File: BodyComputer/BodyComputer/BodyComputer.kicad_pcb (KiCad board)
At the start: 2 copper layers, 0 parts

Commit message: Update due to moving to another computer. Updated Schematic, Print-outs, PCB in development
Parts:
- added BZ1: Buzzer, Buzzer_Beeper:Buzzer_12x9.5RM7.6, F.Cu at (274.8, 30.0)
- added C1: 47u, Capacitor_SMD:CP_Elec_6.3x9.9, F.Cu at (124.5, 141.6)
- added C10: 1u, Capacitor_SMD:C_0603_1608Metric, F.Cu at (89.7, 134.0)
- added C11: 47u, Capacitor_SMD:CP_Elec_6.3x9.9, F.Cu at (140.3, 129.5)
- added C12: 100u, Capacitor_SMD:CP_Elec_6.3x9.9, F.Cu at (70.5, 131.4)
- added C13: 1m, Capacitor_SMD:CP_Elec_10x12.5, F.Cu at (81.3, 130.2)
- added C14: 10n, Capacitor_SMD:C_0603_1608Metric, F.Cu at (382.2, 93.9)
- added C15: 100n, Capacitor_SMD:C_0603_1608Metric, F.Cu at (364.3, 95.7)
- added C16: 1u, Capacitor_SMD:C_0603_1608Metric, F.Cu at (390.7, 87.5)
- added C17: 10n, Capacitor_SMD:C_0603_1608Metric, F.Cu at (368.3, 95.7)
- added C18: 10n, Capacitor_SMD:C_0603_1608Metric, F.Cu at (398.3, 78.4)
- added C19: 100n, Capacitor_SMD:C_0603_1608Metric, F.Cu at (372.3, 95.7)
- added C2: 330u, Capacitor_SMD:CP_Elec_10x12.5, F.Cu at (113.0, 139.7)
- added C20: 100n, Capacitor_SMD:C_0603_1608Metric, F.Cu at (376.3, 95.7)
- added C21: 10n, Capacitor_SMD:C_0603_1608Metric, F.Cu at (217.9, 82.6)
- added C22: 100n, Capacitor_SMD:C_0603_1608Metric, F.Cu at (221.9, 82.6)
- added C23: 1u, Capacitor_SMD:C_0603_1608Metric, F.Cu at (213.9, 82.6)
- added C24: 100n, Capacitor_SMD:C_0603_1608Metric, F.Cu at (225.9, 82.6)
- added C25: 10n, Capacitor_SMD:C_0603_1608Metric, F.Cu at (386.8, 114.4)
- added C26: 100n, Capacitor_SMD:C_0603_1608Metric, F.Cu at (382.7, 114.4)
- added C27: 1u, Capacitor_SMD:C_0603_1608Metric, F.Cu at (382.7, 116.9)
- added C28: 10n, Capacitor_SMD:C_0603_1608Metric, F.Cu at (395.6, 107.2)
- added C29: 100n, Capacitor_SMD:C_0603_1608Metric, F.Cu at (399.6, 104.7)
- added C3: 100n, Capacitor_SMD:C_0603_1608Metric, F.Cu at (133.3, 142.9)
- added C30: 1u, Capacitor_SMD:C_0603_1608Metric, F.Cu at (386.8, 116.9)
- added C31: 10p, Capacitor_SMD:C_0603_1608Metric, F.Cu at (391.5, 111.8)
- added C32: 10p, Capacitor_SMD:C_0603_1608Metric, F.Cu at (381.1, 123.1)
- added C33: 100n, Capacitor_SMD:C_0603_1608Metric, F.Cu at (385.4, 119.5)
- added C34: 100n, Capacitor_SMD:C_0603_1608Metric, F.Cu at (395.5, 112.2)
- added C35: 100n, Capacitor_SMD:C_0603_1608Metric, F.Cu at (387.5, 111.8)
- added C36: 100n, Capacitor_SMD:C_0603_1608Metric, F.Cu at (395.5, 109.7)
- added C37: 100n, Capacitor_SMD:C_0603_1608Metric, F.Cu at (399.6, 107.2)
- added C38: 100n, Capacitor_SMD:C_0603_1608Metric, F.Cu at (342.3, 110.0)
- added C39: 100n, Capacitor_SMD:C_0603_1608Metric, F.Cu at (352.8, 99.0)
- added C4: 100n, Capacitor_SMD:C_0603_1608Metric, F.Cu at (130.2, 142.9)
- added C40: 100n, Capacitor_SMD:C_0603_1608Metric, F.Cu at (346.3, 107.5)
- added C41: 100n, Capacitor_SMD:C_0603_1608Metric, F.Cu at (340.2, 113.2)
- added C42: 100n, Capacitor_SMD:C_0603_1608Metric, F.Cu at (333.3, 117.8)
- added C43: 100n, Capacitor_SMD:C_0603_1608Metric, F.Cu at (342.3, 107.5)
- added C44: 100n, Capacitor_SMD:C_0603_1608Metric, F.Cu at (351.2, 94.0)
- added C45: 100n, Capacitor_SMD:C_0603_1608Metric, F.Cu at (344.8, 99.9)
- added C46: 100n, Capacitor_SMD:C_0603_1608Metric, F.Cu at (332.2, 112.8)
- added C47: 100n, Capacitor_SMD:C_0603_1608Metric, F.Cu at (338.3, 105.7)
- added C48: 100n, Capacitor_SMD:C_0603_1608Metric, F.Cu at (348.8, 97.0)
- added C49: 100n, Capacitor_SMD:C_0603_1608Metric, F.Cu at (338.3, 108.2)
- added C5: 1u, Capacitor_SMD:C_0603_1608Metric, F.Cu at (130.2, 139.1)
- added C50: 100n, Capacitor_SMD:C_0603_1608Metric, F.Cu at (348.8, 102.0)
- added C51: 100n, Capacitor_SMD:C_0603_1608Metric, F.Cu at (332.2, 115.3)
- added C52: 100n, Capacitor_SMD:C_0603_1608Metric, F.Cu at (344.8, 102.4)
- added C6: 10n, Capacitor_SMD:C_0603_1608Metric, F.Cu at (89.7, 130.8)
- added C7: 100n, Capacitor_SMD:C_0603_1608Metric, F.Cu at (133.3, 139.7)
- added C8: 100n, Capacitor_SMD:C_0603_1608Metric, F.Cu at (89.7, 127.6)
- added C9: 1u, Capacitor_SMD:C_0603_1608Metric, F.Cu at (133.3, 136.5)
- added D1: Transil, Diode_SMD:D_SMB_Handsoldering, F.Cu at (41.3, 141.6)
- added D10: LED, Diode_SMD:D_0603_1608Metric_Pad1.05x0.95mm_HandSolder, F.Cu at (121.9, 129.3)
- added D11: LED, Diode_SMD:D_0603_1608Metric_Pad1.05x0.95mm_HandSolder, F.Cu at (209.7, 82.6)
- added D12: D, Diode_SMD:D_SMA, F.Cu at (35.3, 77.2)
- added D13: D, Diode_SMD:D_SMA, F.Cu at (35.3, 55.4)
- added D14: D, Diode_SMD:D_SMA, F.Cu at (35.3, 84.8)
- added D15: D, Diode_SMD:D_SMA, F.Cu at (35.3, 47.8)
- added D16: D, Diode_SMD:D_SMA, F.Cu at (35.3, 99.5)
- added D17: D, Diode_SMD:D_SMA, F.Cu at (15.0, 37.6)
- added D18: D, Diode_SMD:D_SMA, F.Cu at (35.3, 91.9)
- added D19: D, Diode_SMD:D_SMA, F.Cu at (15.0, 30.0)
- added D2: D, Diode_SMD:D_SMC_Handsoldering, F.Cu at (52.1, 142.2)
- added D20: D, Diode_SMD:D_SMA, F.Cu at (35.3, 70.1)
- added D21: D, Diode_SMD:D_SMA, F.Cu at (35.3, 62.5)
- added D22: D, Diode_SMD:D_SMA, F.Cu at (15.0, 67.1)
- added D23: D_Zener, Diode_SMD:D_SOD-323_HandSoldering, F.Cu at (35.6, 113.0)
- added D24: D_Zener, Diode_SMD:D_SOD-323_HandSoldering, F.Cu at (35.6, 107.4)
- added D25: D, Diode_SMD:D_SMA, F.Cu at (15.0, 59.4)
- added D26: D_Zener, Diode_SMD:D_SOD-323_HandSoldering, F.Cu at (37.1, 29.0)
- added D27: D_Zener, Diode_SMD:D_SOD-323_HandSoldering, F.Cu at (37.1, 34.6)
- added D28: D_Zener, Diode_SMD:D_SOD-323_HandSoldering, F.Cu at (37.1, 40.4)
- added D29: D, Diode_SMD:D_SMA, F.Cu at (15.0, 81.8)
- added D3: D_Zener, Diode_SMD:D_SOD-323_HandSoldering, F.Cu at (40.0, 132.7)
- added D30: D, Diode_SMD:D_SMA, F.Cu at (15.0, 74.2)
- added D31: D, Diode_SMD:D_SMA, F.Cu at (15.0, 52.3)
- added D32: D_Zener, Diode_SMD:D_SOD-323_HandSoldering, F.Cu at (54.9, 29.0)
- added D33: D_Zener, Diode_SMD:D_SOD-323_HandSoldering, F.Cu at (54.9, 34.6)
- added D34: D_Zener, Diode_SMD:D_SOD-323_HandSoldering, F.Cu at (54.9, 40.4)
- added D35: D, Diode_SMD:D_SMA, F.Cu at (15.0, 44.7)
- added D36: LED, Diode_SMD:D_0603_1608Metric_Pad1.05x0.95mm_HandSolder, F.Cu at (383.3, 109.4)
- added D37: LED, Diode_SMD:D_0603_1608Metric_Pad1.05x0.95mm_HandSolder, F.Cu at (369.2, 120.6)
- added D38: LED, Diode_SMD:D_0603_1608Metric_Pad1.05x0.95mm_HandSolder, F.Cu at (360.5, 120.6)
- added D39: LED, Diode_SMD:D_0603_1608Metric_Pad1.05x0.95mm_HandSolder, F.Cu at (379.0, 109.4)
- added D4: D, Diode_SMD:D_SMC_Handsoldering, F.Cu at (67.3, 142.2)
- added D40: LED, Diode_SMD:D_0603_1608Metric_Pad1.05x0.95mm_HandSolder, F.Cu at (364.9, 120.6)
- added D41: LED, Diode_SMD:D_0603_1608Metric_Pad1.05x0.95mm_HandSolder, F.Cu at (360.5, 123.2)
- added D42: LED, Diode_SMD:D_0603_1608Metric_Pad1.05x0.95mm_HandSolder, F.Cu at (395.8, 102.1)
- added D43: LED, Diode_SMD:D_0603_1608Metric_Pad1.05x0.95mm_HandSolder, F.Cu at (364.9, 123.2)
- added D44: D_Zener_3V3, Diode_SMD:D_SOD-323_HandSoldering, F.Cu at (325.7, 107.5)
- added D45: D_Zener_3V3, Diode_SMD:D_SOD-323_HandSoldering, F.Cu at (332.2, 101.3)
- added D46: D_Zener_3V3, Diode_SMD:D_SOD-323_HandSoldering, F.Cu at (343.7, 89.2)
- added D47: D_Zener_3V3, Diode_SMD:D_SOD-323_HandSoldering, F.Cu at (338.6, 89.2)
- added D48: D_Zener_3V3, Diode_SMD:D_SOD-323_HandSoldering, F.Cu at (302.6, 118.3)
- added D49: D_Zener_3V3, Diode_SMD:D_SOD-323_HandSoldering, F.Cu at (307.7, 118.3)
- added D5: D, Diode_SMD:D_SMC_Handsoldering, F.Cu at (82.5, 142.2)
- added D50: D_Zener_3V3, Diode_SMD:D_SOD-323_HandSoldering, F.Cu at (320.7, 107.5)
- added D51: D_Zener_3V3, Diode_SMD:D_SOD-323_HandSoldering, F.Cu at (332.2, 98.4)
- added D52: D_Zener_3V3, Diode_SMD:D_SOD-323_HandSoldering, F.Cu at (338.6, 92.2)
- added D53: D_Zener_3V3, Diode_SMD:D_SOD-323_HandSoldering, F.Cu at (297.6, 118.3)
- added D54: D_Zener_3V3, Diode_SMD:D_SOD-323_HandSoldering, F.Cu at (320.7, 110.5)
- added D55: D_Zener_3V3, Diode_SMD:D_SOD-323_HandSoldering, F.Cu at (312.7, 118.3)
- added D56: D_Zener, Diode_SMD:D_SOD-323_HandSoldering, F.Cu at (63.2, 92.7)
- added D57: D_Zener, Diode_SMD:D_SOD-323_HandSoldering, F.Cu at (63.2, 98.1)
- added D6: D, Diode_SMD:D_SMC_Handsoldering, F.Cu at (97.8, 142.2)
- added D7: D_Zener, Diode_SMD:D_SOD-323_HandSoldering, F.Cu at (134.0, 128.9)
- added D8: LED, Diode_SMD:D_0603_1608Metric_Pad1.05x0.95mm_HandSolder, F.Cu at (125.7, 129.3)
- added D9: LED, Diode_SMD:D_0603_1608Metric_Pad1.05x0.95mm_HandSolder, F.Cu at (129.5, 129.3)
- added F1: Fuse, SamacSys_Parts:FuseHolder22mm, F.Cu at (35.6, 143.5)
- added J1: Screw_Terminal_01x02, SamacSys_Parts:SHDR2W99P0X500_1X2_1000X760X1000P, F.Cu at (7.62, 136.5)
- added J10: Conn_02x03_Odd_Even, Connector_IDC:IDC-Header_2x03_P2.54mm_Vertical, F.Cu at (254.1, 53.2)
- added J11: SS-6488-FLS, SamacSys_Parts:SS6488FLS, F.Cu at (165.4, 84.3)
- added J12: USB_B_Mini, Connector_USB:USB_Mini-B_Wuerth_65100516121_Horizontal, F.Cu at (245.6, 74.1)
- added J13: Conn_02x05_Odd_Even, Connector_IDC:IDC-Header_2x05_P2.54mm_Vertical, F.Cu at (265.3, 51.6)
- added J14: Conn_02x05_Odd_Even, Connector_IDC:IDC-Header_2x05_P2.54mm_Vertical, F.Cu at (265.3, 29.4)
- added J15: Screw_Terminal_01x02, SamacSys_Parts:SHDR2W99P0X500_1X2_1000X760X1000P, F.Cu at (27.9, 78.5)
- added J16: Screw_Terminal_01x02, SamacSys_Parts:SHDR2W99P0X500_1X2_1000X760X1000P, F.Cu at (27.9, 54.1)
- added J17: Screw_Terminal_01x02, SamacSys_Parts:SHDR2W99P0X500_1X2_1000X760X1000P, F.Cu at (27.9, 98.3)
- added J18: Screw_Terminal_01x02, SamacSys_Parts:SHDR2W99P0X500_1X2_1000X760X1000P, F.Cu at (7.62, 36.3)
- added J19: Screw_Terminal_01x02, SamacSys_Parts:SHDR2W99P0X500_1X2_1000X760X1000P, F.Cu at (48.5, 112.3)
- added J2: Screw_Terminal_01x02, SamacSys_Parts:SHDR2W99P0X500_1X2_1000X760X1000P, F.Cu at (7.62, 125.7)
- added J20: Screw_Terminal_01x02, SamacSys_Parts:SHDR2W99P0X500_1X2_1000X760X1000P, F.Cu at (27.9, 68.8)
- added J21: Screw_Terminal_01x02, SamacSys_Parts:SHDR2W99P0X500_1X2_1000X760X1000P, F.Cu at (54.4, 98.4)
- added J22: Screw_Terminal_01x03, SamacSys_Parts:SHDR3W95P0X500_1X3_1620X900X1280P, F.Cu at (27.9, 40.1)
- added J23: Screw_Terminal_01x02, SamacSys_Parts:SHDR2W99P0X500_1X2_1000X760X1000P, F.Cu at (7.62, 65.8)
- added J24: Screw_Terminal_01x02, SamacSys_Parts:SHDR2W99P0X500_1X2_1000X760X1000P, F.Cu at (7.62, 80.5)
- added J25: Screw_Terminal_01x03, SamacSys_Parts:SHDR3W95P0X500_1X3_1620X900X1280P, F.Cu at (45.5, 40.1)
- added J26: Screw_Terminal_01x02, SamacSys_Parts:SHDR2W99P0X500_1X2_1000X760X1000P, F.Cu at (7.62, 51.1)
- added J27: Screw_Terminal_01x02, SamacSys_Parts:SHDR2W99P0X500_1X2_1000X760X1000P, F.Cu at (298.3, 103.1)
- added J28: Screw_Terminal_01x02, SamacSys_Parts:SHDR2W99P0X500_1X2_1000X760X1000P, F.Cu at (316.3, 92.3)
- added J29: Screw_Terminal_01x02, SamacSys_Parts:SHDR2W99P0X500_1X2_1000X760X1000P, F.Cu at (298.3, 112.2)
- added J3: Screw_Terminal_01x03, SamacSys_Parts:SHDR3W95P0X500_1X3_1620X900X1280P, F.Cu at (7.62, 114.3)
- added J30: Screw_Terminal_01x02, SamacSys_Parts:SHDR2W99P0X500_1X2_1000X760X1000P, F.Cu at (309.9, 103.1)
- added J31: Screw_Terminal_01x02, SamacSys_Parts:SHDR2W99P0X500_1X2_1000X760X1000P, F.Cu at (327.8, 92.3)
- added J32: Screw_Terminal_01x03, SamacSys_Parts:SHDR3W95P0X500_1X3_1620X900X1280P, F.Cu at (299.1, 93.5)
- added J33: Screw_Terminal_01x02, SamacSys_Parts:SHDR2W99P0X500_1X2_1000X760X1000P, F.Cu at (309.9, 112.2)
- added J34: Screw_Terminal_01x02, SamacSys_Parts:SHDR2W99P0X500_1X2_1000X760X1000P, F.Cu at (321.4, 101.5)
- added J35: Conn_01x02, Connector_PinSocket_2.54mm:PinSocket_1x02_P2.54mm_Vertical, F.Cu at (-6.86, 132.3)
- added J4: Screw_Terminal_01x03, SamacSys_Parts:SHDR3W95P0X500_1X3_1620X900X1280P, F.Cu at (7.62, 97.2)
- added J5: Screw_Terminal_01x03, SamacSys_Parts:SHDR3W95P0X500_1X3_1620X900X1280P, F.Cu at (27.9, 132.7)
- added J6: Screw_Terminal_01x03, SamacSys_Parts:SHDR3W95P0X500_1X3_1620X900X1280P, F.Cu at (27.9, 114.9)
- added J7: MicroSD, SamacSys_Parts:1140084168, F.Cu at (388.2, 78.5)
- added J8: SS-6488-FLS, SamacSys_Parts:SS6488FLS, F.Cu at (94.5, 33.3)
- added J9: Conn_02x05_Odd_Even, Connector_IDC:IDC-Header_2x05_P2.54mm_Vertical, F.Cu at (243.4, 53.2)
- added Q1: Q_NPN_BCE, Package_TO_SOT_SMD:SOT-23, F.Cu at (287.6, 25.5)
- added Q10: IRLML2060, Package_TO_SOT_SMD:SOT-23, F.Cu at (39.4, 68.6)
- added Q11: IRLML2060, Package_TO_SOT_SMD:SOT-23, F.Cu at (39.4, 61.0)
- added Q12: IRLML2060, Package_TO_SOT_SMD:SOT-23, F.Cu at (19.1, 65.5)
- added Q13: IRLML2060, Package_TO_SOT_SMD:SOT-23, F.Cu at (19.1, 57.9)
- added Q14: IRLML2060, Package_TO_SOT_SMD:SOT-23, F.Cu at (19.1, 80.3)
- added Q15: IRLML2060, Package_TO_SOT_SMD:SOT-23, F.Cu at (19.1, 72.6)
- added Q16: IRLML2060, Package_TO_SOT_SMD:SOT-23, F.Cu at (19.1, 50.8)
- added Q17: IRLML2060, Package_TO_SOT_SMD:SOT-23, F.Cu at (19.1, 43.2)
- added Q2: IRLML2060, Package_TO_SOT_SMD:SOT-23, F.Cu at (39.4, 75.7)
- added Q3: IRLML2060, Package_TO_SOT_SMD:SOT-23, F.Cu at (39.4, 53.8)
- added Q4: IRLML2060, Package_TO_SOT_SMD:SOT-23, F.Cu at (39.4, 83.3)
- added Q5: IRLML2060, Package_TO_SOT_SMD:SOT-23, F.Cu at (39.4, 46.2)
- added Q6: IRLML2060, Package_TO_SOT_SMD:SOT-23, F.Cu at (39.4, 98.0)
- added Q7: IRLML2060, Package_TO_SOT_SMD:SOT-23, F.Cu at (19.1, 36.1)
- added Q8: IRLML2060, Package_TO_SOT_SMD:SOT-23, F.Cu at (39.6, 90.4)
- added Q9: IRLML2060, Package_TO_SOT_SMD:SOT-23, F.Cu at (19.1, 28.4)
- added R1: 4,7k, Resistor_SMD:R_0603_1608Metric, F.Cu at (35.6, 134.0)
- added R10: 1,6k, Resistor_SMD:R_0603_1608Metric, F.Cu at (126.4, 133.3)
- added R100: 100, Resistor_SMD:R_0603_1608Metric, F.Cu at (19.8, 46.7)
- added R101: 10k, Resistor_SMD:R_0603_1608Metric, F.Cu at (21.6, 43.2)
- added R102: 56, Resistor_SMD:R_0603_1608Metric, F.Cu at (325.3, 118.2)
- added R103: 300, Resistor_SMD:R_0603_1608Metric, F.Cu at (351.2, 91.5)
- added R104: 300, Resistor_SMD:R_0603_1608Metric, F.Cu at (344.8, 97.4)
- added R105: 300, Resistor_SMD:R_0603_1608Metric, F.Cu at (328.2, 112.8)
- added R106: 300, Resistor_SMD:R_0603_1608Metric, F.Cu at (334.2, 106.6)
- added R107: 300, Resistor_SMD:R_0603_1608Metric, F.Cu at (346.1, 94.5)
- added R108: 300, Resistor_SMD:R_0603_1608Metric, F.Cu at (324.1, 115.7)
- added R109: 300, Resistor_SMD:R_0603_1608Metric, F.Cu at (330.2, 107.3)
- added R11: 560, Resistor_SMD:R_0603_1608Metric, F.Cu at (130.8, 133.3)
- added R110: 300, Resistor_SMD:R_0603_1608Metric, F.Cu at (340.7, 99.9)
- added R111: 10k, Resistor_SMD:R_0603_1608Metric, F.Cu at (352.2, 89.0)
- added R112: NULL, Resistor_SMD:R_0603_1608Metric, F.Cu at (329.2, 110.3)
- added R113: 10k, Resistor_SMD:R_0603_1608Metric, F.Cu at (336.7, 98.2)
- added R114: 10k, Resistor_SMD:R_0603_1608Metric, F.Cu at (328.2, 115.3)
- added R115: 10k, Resistor_SMD:R_0603_1608Metric, F.Cu at (317.2, 118.2)
- added R116: 10k, Resistor_SMD:R_0603_1608Metric, F.Cu at (340.7, 97.4)
- added R117: 10k, Resistor_SMD:R_0603_1608Metric, F.Cu at (336.7, 100.7)
- added R118: 1k, Resistor_SMD:R_0603_1608Metric, F.Cu at (324.1, 113.2)
- added R119: 1k, Resistor_SMD:R_0603_1608Metric, F.Cu at (336.7, 103.2)
- added R12: 200, Resistor_SMD:R_0603_1608Metric, F.Cu at (120.7, 133.3)
- added R120: 1k, Resistor_SMD:R_0603_1608Metric, F.Cu at (334.2, 109.1)
- added R121: 1k, Resistor_SMD:R_0603_1608Metric, F.Cu at (347.1, 92.0)
- added R122: 10k, Resistor_SMD:R_0603_1608Metric, F.Cu at (325.2, 110.3)
- added R123: 10k, Resistor_SMD:R_0603_1608Metric, F.Cu at (331.7, 104.1)
- added R124: 10k, Resistor_SMD:R_0603_1608Metric, F.Cu at (320.1, 115.7)
- added R125: 10k, Resistor_SMD:R_0603_1608Metric, F.Cu at (321.2, 118.2)
- added R126: 10k, Resistor_SMD:R_0603_1608Metric, F.Cu at (346.3, 104.9)
- added R127: 10k, Resistor_SMD:R_0603_1608Metric, F.Cu at (333.3, 120.3)
- added R128: 10k, Resistor_SMD:R_0603_1608Metric, F.Cu at (337.3, 115.7)
- added R129: 10k, Resistor_SMD:R_0603_1608Metric, F.Cu at (352.8, 101.6)
- added R13: 47k, Resistor_SMD:R_0603_1608Metric, F.Cu at (380.3, 96.4)
- added R130: 1k, Resistor_SMD:R_0603_1608Metric, F.Cu at (350.3, 104.5)
- added R131: 1k, Resistor_SMD:R_0603_1608Metric, F.Cu at (336.2, 113.2)
- added R132: 1k, Resistor_SMD:R_0603_1608Metric, F.Cu at (320.1, 113.2)
- added R133: 1k, Resistor_SMD:R_0603_1608Metric, F.Cu at (338.1, 94.9)
- added R134: 10k, Resistor_SMD:R_0603_1608Metric, F.Cu at (343.1, 92.0)
- added R135: 10k, Resistor_SMD:R_0603_1608Metric, F.Cu at (348.2, 89.0)
- added R136: 10k, Resistor_SMD:R_0603_1608Metric, F.Cu at (342.1, 94.9)
- added R137: 10k, Resistor_SMD:R_0603_1608Metric, F.Cu at (329.3, 117.8)
- added R138: 10k, Resistor_SMD:R_0603_1608Metric, F.Cu at (329.3, 120.3)
- added R139: 10k, Resistor_SMD:R_0603_1608Metric, F.Cu at (340.7, 102.4)
- added R14: 47k, Resistor_SMD:R_0603_1608Metric, F.Cu at (386.2, 93.9)
- added R140: 10k, Resistor_SMD:R_0603_1608Metric, F.Cu at (352.8, 96.5)
- added R141: 10k, Resistor_SMD:R_0603_1608Metric, F.Cu at (342.3, 104.9)
- added R142: 1k, Resistor_SMD:R_0603_1608Metric, F.Cu at (348.8, 99.5)
- added R143: 1k, Resistor_SMD:R_0603_1608Metric, F.Cu at (338.3, 110.7)
- added R144: 10k, Resistor_SMD:R_0603_1608Metric, F.Cu at (134.6, -77.7)
- added R145: 10k, Resistor_SMD:R_0603_1608Metric, F.Cu at (134.6, -75.2)
- added R146: 10k, Resistor_SMD:R_0603_1608Metric, F.Cu at (138.6, -77.7)
- added R147: 10k, Resistor_SMD:R_0603_1608Metric, F.Cu at (134.6, -72.7)
- added R148: 1k, Resistor_SMD:R_0603_1608Metric, F.Cu at (138.6, -75.2)
- added R149: 10k, Resistor_SMD:R_0603_1608Metric, F.Cu at (142.6, -77.7)
- added R15: 47k, Resistor_SMD:R_0603_1608Metric, F.Cu at (398.3, 80.9)
- added R150: 1k, Resistor_SMD:R_0603_1608Metric, F.Cu at (134.6, -70.2)
- added R151: 1k, Resistor_SMD:R_0603_1608Metric, F.Cu at (138.6, -72.7)
- added R152: 10k, Resistor_SMD:R_0603_1608Metric, F.Cu at (142.6, -75.2)
- added R153: 10k, Resistor_SMD:R_0603_1608Metric, F.Cu at (146.6, -77.7)
- added R154: 10k, Resistor_SMD:R_0603_1608Metric, F.Cu at (138.6, -70.2)
- added R155: 10k, Resistor_SMD:R_0603_1608Metric, F.Cu at (142.6, -72.7)
- added R156: 1k, Resistor_SMD:R_0603_1608Metric, F.Cu at (146.6, -75.2)
- added R157: 1k, Resistor_SMD:R_0603_1608Metric, F.Cu at (142.6, -70.2)
- added R158: 10k, Resistor_SMD:R_0603_1608Metric, F.Cu at (146.6, -72.7)
- added R159: 10k, Resistor_SMD:R_0603_1608Metric, F.Cu at (146.6, -70.2)
- added R16: 47k, Resistor_SMD:R_0603_1608Metric, F.Cu at (398.7, 85.9)
- added R160: 0, Resistor_SMD:R_0603_1608Metric, F.Cu at (60.7, 92.5)
- added R161: 0, Resistor_SMD:R_0603_1608Metric, F.Cu at (60.7, 97.8)
- added R17: 47k, Resistor_SMD:R_0603_1608Metric, F.Cu at (360.2, 95.7)
- added R18: NULL, Resistor_SMD:R_0603_1608Metric, F.Cu at (390.7, 90.0)
- added R19: NULL, Resistor_SMD:R_0603_1608Metric, F.Cu at (394.7, 87.5)
- added R2: 10k, Resistor_SMD:R_0603_1608Metric, F.Cu at (373.6, 60.8)
- added R20: NULL, Resistor_SMD:R_0603_1608Metric, F.Cu at (394.7, 90.0)
- added R21: NULL, Resistor_SMD:R_0603_1608Metric, F.Cu at (402.3, 78.4)
- added R22: NULL, Resistor_SMD:R_0603_1608Metric, F.Cu at (384.3, 96.4)
- added R23: NULL, Resistor_SMD:R_0603_1608Metric, F.Cu at (398.3, 83.4)
- added R24: NULL, Resistor_SMD:R_0603_1608Metric, F.Cu at (390.2, 93.9)
- added R25: NULL, Resistor_SMD:R_0603_1608Metric, F.Cu at (402.3, 80.9)
- added R26: 1k, Resistor_SMD:R_0603_1608Metric, F.Cu at (291.9, 24.5)
- added R27: 200, Resistor_SMD:R_0603_1608Metric, F.Cu at (238.0, 82.6)
- added R28: 1k, Resistor_SMD:R_0603_1608Metric, F.Cu at (234.0, 82.6)
- added R29: 10k, Resistor_SMD:R_0603_1608Metric, F.Cu at (229.9, 82.6)
- added R3: 1k, Resistor_SMD:R_0603_1608Metric, F.Cu at (35.6, 130.2)
- added R30: 10k, Resistor_SMD:R_0603_1608Metric, F.Cu at (41.9, 75.7)
- added R31: 10k, Resistor_SMD:R_0603_1608Metric, F.Cu at (41.9, 53.8)
- added R32: 100, Resistor_SMD:R_0603_1608Metric, F.Cu at (38.6, 79.2)
- added R33: 100, Resistor_SMD:R_0603_1608Metric, F.Cu at (40.1, 57.4)
- added R34: 0, Resistor_SMD:R_0603_1608Metric, F.Cu at (40.1, 79.2)
- added R35: 0, Resistor_SMD:R_0603_1608Metric, F.Cu at (38.6, 57.4)
- added R36: 0, Resistor_SMD:R_0603_1608Metric, F.Cu at (38.6, 86.9)
- added R37: 0, Resistor_SMD:R_0603_1608Metric, F.Cu at (38.6, 49.8)
- added R38: 100, Resistor_SMD:R_0603_1608Metric, F.Cu at (40.1, 86.9)
- added R39: 100, Resistor_SMD:R_0603_1608Metric, F.Cu at (40.1, 49.8)
- added R4: 10k, Resistor_SMD:R_0603_1608Metric, F.Cu at (394.1, 40.4)
- added R40: 0, Resistor_SMD:R_0603_1608Metric, F.Cu at (41.9, 112.5)
- added R41: 1k, Resistor_SMD:R_0603_1608Metric, F.Cu at (48.3, 119.4)
- added R42: 0, Resistor_SMD:R_0603_1608Metric, F.Cu at (41.9, 106.9)
- added R43: 1k, Resistor_SMD:R_0603_1608Metric, F.Cu at (48.3, 121.2)
- added R44: 10k, Resistor_SMD:R_0603_1608Metric, F.Cu at (41.9, 83.3)
- added R45: 10k, Resistor_SMD:R_0603_1608Metric, F.Cu at (41.9, 46.3)
- added R46: 10k, Resistor_SMD:R_0603_1608Metric, F.Cu at (41.9, 98.0)
- added R47: 10k, Resistor_SMD:R_0603_1608Metric, F.Cu at (21.6, 36.1)
- added R48: 3k, Resistor_SMD:R_0603_1608Metric, F.Cu at (48.3, 117.9)
- added R49: 3k, Resistor_SMD:R_0603_1608Metric, F.Cu at (48.3, 122.7)
- added R5: 1,6k, Resistor_SMD:R_0603_1608Metric, F.Cu at (134.0, 133.3)
- added R50: 100, Resistor_SMD:R_0603_1608Metric, F.Cu at (40.1, 101.6)
- added R51: 100, Resistor_SMD:R_0603_1608Metric, F.Cu at (19.8, 39.6)
- added R52: 0, Resistor_SMD:R_0603_1608Metric, F.Cu at (38.6, 101.6)
- added R53: 0, Resistor_SMD:R_0603_1608Metric, F.Cu at (18.3, 39.6)
- added R54: 0, Resistor_SMD:R_0603_1608Metric, F.Cu at (38.9, 94.0)
- added R55: 0, Resistor_SMD:R_0603_1608Metric, F.Cu at (18.3, 32.0)
- added R56: 100, Resistor_SMD:R_0603_1608Metric, F.Cu at (40.4, 94.0)
- added R57: 100, Resistor_SMD:R_0603_1608Metric, F.Cu at (19.8, 32.0)
- added R58: 10k, Resistor_SMD:R_0603_1608Metric, F.Cu at (21.6, 28.4)
- added R59: 10k, Resistor_SMD:R_0603_1608Metric, F.Cu at (42.2, 90.4)
- added R6: 1,6k, Resistor_SMD:R_0603_1608Metric, F.Cu at (133.5, 125.1)
- added R60: 10k, Resistor_SMD:R_0603_1608Metric, F.Cu at (41.9, 68.6)
- added R61: 100, Resistor_SMD:R_0603_1608Metric, F.Cu at (40.1, 72.2)
- added R62: 0, Resistor_SMD:R_0603_1608Metric, F.Cu at (38.6, 72.2)
- added R63: 0, Resistor_SMD:R_0603_1608Metric, F.Cu at (38.6, 64.5)
- added R64: 100, Resistor_SMD:R_0603_1608Metric, F.Cu at (40.1, 64.5)
- added R65: 10k, Resistor_SMD:R_0603_1608Metric, F.Cu at (41.9, 61.0)
- added R66: 10k, Resistor_SMD:R_0603_1608Metric, F.Cu at (21.6, 65.5)
- added R67: 0, Resistor_SMD:R_0603_1608Metric, F.Cu at (39.6, 111.8)
- added R68: 0, Resistor_SMD:R_0603_1608Metric, F.Cu at (39.6, 113.3)
- added R69: 0, Resistor_SMD:R_0603_1608Metric, F.Cu at (39.6, 107.7)
- added R7: 0, Resistor_SMD:R_0603_1608Metric, F.Cu at (60.7, 93.9)
- added R70: 0, Resistor_SMD:R_0603_1608Metric, F.Cu at (39.6, 106.2)
- added R71: 100, Resistor_SMD:R_0603_1608Metric, F.Cu at (19.8, 69.1)
- added R72: 0, Resistor_SMD:R_0603_1608Metric, F.Cu at (18.3, 69.1)
- added R73: 0, Resistor_SMD:R_0603_1608Metric, F.Cu at (37.3, 112.5)
- added R74: 0, Resistor_SMD:R_0603_1608Metric, F.Cu at (37.3, 106.9)
- added R75: 0, Resistor_SMD:R_0603_1608Metric, F.Cu at (18.3, 61.5)
- added R76: 0, Resistor_SMD:R_0603_1608Metric, F.Cu at (34.5, 30.2)
- added R77: 0, Resistor_SMD:R_0603_1608Metric, F.Cu at (34.6, 35.8)
- added R78: 0, Resistor_SMD:R_0603_1608Metric, F.Cu at (34.5, 41.7)
- added R79: 100, Resistor_SMD:R_0603_1608Metric, F.Cu at (19.8, 61.5)
- added R8: 0, Resistor_SMD:R_0603_1608Metric, F.Cu at (60.7, 99.3)
- added R80: 10k, Resistor_SMD:R_0603_1608Metric, F.Cu at (21.6, 57.9)
- added R81: 0, Resistor_SMD:R_0603_1608Metric, F.Cu at (34.5, 28.7)
- added R82: 0, Resistor_SMD:R_0603_1608Metric, F.Cu at (34.5, 34.3)
- added R83: 0, Resistor_SMD:R_0603_1608Metric, F.Cu at (34.5, 40.1)
- added R84: 10k, Resistor_SMD:R_0603_1608Metric, F.Cu at (21.6, 80.3)
- added R85: 100, Resistor_SMD:R_0603_1608Metric, F.Cu at (19.8, 83.8)
- added R86: 0, Resistor_SMD:R_0603_1608Metric, F.Cu at (18.3, 83.8)
- added R87: 0, Resistor_SMD:R_0603_1608Metric, F.Cu at (18.3, 76.2)
- added R88: 100, Resistor_SMD:R_0603_1608Metric, F.Cu at (19.8, 76.2)
- added R89: 10k, Resistor_SMD:R_0603_1608Metric, F.Cu at (21.6, 72.6)
- added R9: 1,6k, Resistor_SMD:R_0603_1608Metric, F.Cu at (124.5, 133.3)
- added R90: 10k, Resistor_SMD:R_0603_1608Metric, F.Cu at (21.6, 50.8)
- added R91: 100, Resistor_SMD:R_0603_1608Metric, F.Cu at (19.8, 54.4)
- added R92: 0, Resistor_SMD:R_0603_1608Metric, F.Cu at (52.3, 30.2)
- added R93: 0, Resistor_SMD:R_0603_1608Metric, F.Cu at (52.3, 35.8)
- added R94: 0, Resistor_SMD:R_0603_1608Metric, F.Cu at (52.3, 41.7)
- added R95: 0, Resistor_SMD:R_0603_1608Metric, F.Cu at (18.3, 54.4)
- added R96: 0, Resistor_SMD:R_0603_1608Metric, F.Cu at (18.3, 46.7)
- added R97: 0, Resistor_SMD:R_0603_1608Metric, F.Cu at (52.3, 28.7)
- added R98: 0, Resistor_SMD:R_0603_1608Metric, F.Cu at (52.3, 34.3)
- added R99: 0, Resistor_SMD:R_0603_1608Metric, F.Cu at (52.3, 40.1)
- added SW1: SW_Push, Button_Switch_THT:SW_PUSH_6mm, F.Cu at (254.0, 69.7)
- added TH1: NTC_100k, Resistor_SMD:R_0402_1005Metric, F.Cu at (342.0, 66.3)
- added TH2: NTC_100k, Resistor_SMD:R_0402_1005Metric, F.Cu at (339.1, 66.3)
- added TP1: TestPoint_Flag, TestPoint:TestPoint_Pad_D1.0mm, F.Cu at (389.0, 119.6)
- added TP2: TestPoint_Flag, TestPoint:TestPoint_Pad_D1.0mm, F.Cu at (399.1, 110.0)
- added TP3: TestPoint_Flag, TestPoint:TestPoint_Pad_D1.0mm, F.Cu at (394.3, 115.0)
- added TP4: TestPoint_Flag, TestPoint:TestPoint_Pad_D1.0mm, F.Cu at (388.6, 122.7)
- added U1: AZ1117-3.3, Package_TO_SOT_SMD:SOT-223, F.Cu at (98.4, 130.8)
- added U2: AZ1117-5.0, Package_TO_SOT_SMD:SOT-223, F.Cu at (140.3, 140.3)
- added U3: EEPROM, Package_SO:SO-8_3.9x4.9mm_P1.27mm, F.Cu at (384.4, 89.5)
- added U4: EEPROM, Package_SO:SO-8_3.9x4.9mm_P1.27mm, F.Cu at (400.5, 73.9)
- added U5: NodeMCU_1.0_(ESP-12E), ESP8266:NodeMCU-LoLinV3, F.Cu at (223.3, 54.3)
- added U6: LM358, Package_DIP:DIP-8_W7.62mm_Socket_LongPads, F.Cu at (43.9, 118.6)
- added U7: STM32F103VETx, Package_QFP:LQFP-100_14x14mm_P0.5mm, F.Cu at (90.0, 85.0)
- added Y1: 8-16MHz, Crystal:Crystal_SMD_SeikoEpson_MA505-2Pin_12.7x5.1mm, F.Cu at (72.4, 74.9)
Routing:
- net (no net): vias 0 -> 238
- added copper zone on F.Cu, net GND
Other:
- board outline added: 180 x 130 mm

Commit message: Updated schematic (DC/DC), 2-layer PCB
Updated schematic in multiple places, added elements, exchanged 3V3 stabilizer for a DC/DC converter. Nearly finished 2-layer PCB layout.
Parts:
- removed D6: D, Diode_SMD:D_SMC_Handsoldering
- added C53: 100n, Capacitor_SMD:C_0603_1608Metric, F.Cu at (64.2, 136.4)
- added J36: Conn_01x08, Connector_PinHeader_2.54mm:PinHeader_1x08_P2.54mm_Vertical, F.Cu at (125.0, 130.8)
- added J37: Conn_01x02, Connector_PinSocket_2.54mm:PinSocket_1x02_P2.54mm_Vertical, F.Cu at (25.9, 135.0)
- added J38: Conn_01x03, Connector_PinHeader_2.54mm:PinHeader_1x03_P2.54mm_Vertical, F.Cu at (145.0, 71.4)
- added L1: SRN6045TA-6R8M, SamacSys_Parts:SRN6045TA-6R8M, F.Cu at (81.0, 140.8)
- added R162: 10k, Resistor_SMD:R_0603_1608Metric, F.Cu at (82.7, 23.4)
- added R163: 20, Resistor_SMD:R_0603_1608Metric, F.Cu at (128.5, 118.5)
- added R164: 20, Resistor_SMD:R_0603_1608Metric, F.Cu at (128.5, 115.4)
- added R165: 20, Resistor_SMD:R_0603_1608Metric, F.Cu at (128.5, 120.0)
- added R166: 20, Resistor_SMD:R_0603_1608Metric, F.Cu at (128.5, 117.0)
- added R167: 20, Resistor_SMD:R_0603_1608Metric, F.Cu at (128.5, 113.9)
- added R168: 20, Resistor_SMD:R_0603_1608Metric, F.Cu at (128.5, 112.4)
- added R169: 330, Resistor_SMD:R_0603_1608Metric, F.Cu at (140.6, 99.8)
- D1: footprint Diode_SMD:D_SMB_Handsoldering -> Diode_SMD:D_SMB
- D2: footprint Diode_SMD:D_SMC_Handsoldering -> Diode_SMD:D_SMC
- D4: value D -> SSB43L-E3/52T; footprint Diode_SMD:D_SMC_Handsoldering -> Diode_SMD:D_SMB
- D5: value D -> LED; footprint Diode_SMD:D_SMC_Handsoldering -> Diode_SMD:D_0603_1608Metric_Pad1.05x0.95mm_HandSolder
- R102: value 56 -> 56/NULL
- U1: value AZ1117-3.3 -> ADP2302ARDZ-3.3; footprint Package_TO_SOT_SMD:SOT-223 -> Package_SO:SOIC-8-1EP_3.9x4.9mm_P1.27mm_EP2.29x3mm
- U2: footprint Package_TO_SOT_SMD:SOT-223 -> Package_TO_SOT_SMD:SOT-223-3_TabPin2
- moved R14 323.2 mm to (67.9, 37.8), turned to 180 degrees
- moved R4 320.8 mm to (81.8, 113.5), turned to 90 degrees
- moved J7 319.3 mm to (73.0, 27.3)
- moved R13 318.2 mm to (67.9, 36.1), turned to 180 degrees
- moved R16 314.9 mm to (87.8, 36.1)
- moved R15 314.0 mm to (87.8, 34.3)
- moved C16 313.1 mm to (82.5, 31.8)
- moved R21 308.5 mm to (94.4, 59.1), turned to 270 degrees
- moved C14 306.7 mm to (82.5, 28.7)
- moved C29 303.1 mm to (96.6, 111.5), turned to 180 degrees
- moved C31 302.6 mm to (89.5, 93.9)
- moved C37 300.6 mm to (99.2, 97.8), turned to 90 degrees
- moved R25 300.5 mm to (101.9, 72.3), turned to 270 degrees
- moved C28 299.0 mm to (96.6, 113.0), turned to 180 degrees
- moved U4 299.0 mm to (101.6, 65.7), turned to 270 degrees
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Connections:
- D2 pad 1: Net-(D2-Pad1) -> +12V
- D4 pad 1: Net-(D4-Pad1) -> Net-(C53-Pad2)
- D4 pad 2: Net-(D2-Pad1) -> GND
- D5 pad 1: Net-(D5-Pad1) -> GND
- D5 pad 2: Net-(D4-Pad1) -> Net-(D5-Pad2)
- J14 pad 6: /MCU/I2C2_SDA -> /MCU/I2C2_SCL
- J14 pad 8: /MCU/I2C2_SCL -> /MCU/I2C2_SDA
- J7 pad 10: Net-(J7-Pad10) -> GND
- J7 pad 11: Net-(J7-Pad11) -> GND
- J7 pad 12: Net-(J7-Pad12) -> GND
- J7 pad 9: Net-(J7-Pad9) -> GND
- J7 pad CD1: GND -> /MCU/Diag_LED_1
- J7 pad CD2: /Memory/FLASH_DATA_1 -> Net-(J7-PadCD2)
- J8 pad 1: /Memory/FLASH_DATA_0 -> Net-(J8-Pad1)
- J8 pad 2: /Memory/FLASH_DATA_1 -> Net-(J8-Pad2)
- J8 pad 3: /Memory/FLASH_DATA_2 -> Net-(J8-Pad3)
- J8 pad 4: /Memory/FLASH_DATA_3 -> Net-(J8-Pad4)
- J8 pad 5: /Memory/FLASH_DATA_CLK -> Net-(J8-Pad5)
- J8 pad 6: /Memory/FLASH_DATA_CMD -> Net-(J8-Pad6)
- U1 pad 1: GND -> Net-(C53-Pad1)
- U1 pad 2: +3V3 -> +12V
- U1 pad 4: (no net) -> Net-(U1-Pad4)
- U7 pad 3: /GPIO/GPIO_5 -> /GPIO/GPIO_9
- U7 pad 37: Net-(U7-Pad37) -> /Peripherals/BUZZER
- U7 pad 39: /GPIO/GPIO_9 -> /GPIO/GPIO_5
- U7 pad 7: /GPIO/GPIO_10 -> /GPIO/GPIO_11
- U7 pad 8: /GPIO/GPIO_11 -> /GPIO/GPIO_10
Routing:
- net +5V: track 0.00 -> 262.6 mm, vias 0 -> 17
- net /MCU/MOSFET_16: track 0.00 -> 171.5 mm, vias 0 -> 4
- net /MCU/MOSFET_15: track 0.00 -> 163.5 mm, vias 0 -> 4
- net /Inputs_Outputs/MOSFET_OUT_12: track 0.00 -> 156.0 mm, vias 0 -> 4
- net /MCU/Diag_LED_1: track 0.00 -> 153.0 mm, vias 0 -> 5
- net /Inputs_Outputs/MOSFET_OUT_11: track 0.00 -> 149.3 mm, vias 0 -> 4
- net /Inputs_Outputs/MOSFET_OUT_14: track 0.00 -> 136.2 mm, vias 0 -> 4
- net GND: track 0.00 -> 131.0 mm, vias 0 -> 479
- net /Inputs_Outputs/MOSFET_OUT_10: track 0.00 -> 130.8 mm, vias 0 -> 8
- net /Inputs_Outputs/MOSFET_OUT_13: track 0.00 -> 127.8 mm, vias 0 -> 5
- net /Memory/FLASH_DATA_0: track 0.00 -> 127.4 mm, vias 0 -> 4
- net /Memory/FLASH_DATA_1: track 0.00 -> 127.0 mm, vias 0 -> 4
- net /Inputs_Outputs/MOSFET_OUT_1: track 0.00 -> 125.5 mm, vias 0 -> 6
- net +3V3: track 0.00 -> 124.4 mm, vias 0 -> 99
- net /Inputs_Outputs/MOSFET_OUT_9: track 0.00 -> 122.1 mm, vias 0 -> 8
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- added copper zone on B.Cu, net +3V3
- added copper zone on F.Cu, net +3V3
- added copper zone on B.Cu, net +5V
- added copper zone on F.Cu, net +5V
- added copper zone on B.Cu, net GND
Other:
- board size 180 x 130 mm -> 151.5 x 130 mm
- net class Default: clearance 0.2 -> 0.1524; trace_width 0.25 -> 0.1524; via_dia 0.8 -> 0.6; via_drill 0.4 -> 0.3
- rule trace_clearance: 0.2 -> 0.1524
- rule trace_min: 0.2 -> 0.1524
- rule via_min_size: 0.4 -> 0.6
- board text added: "1"
- board text added: "12V"
- board text added: "2"
- board text added: "3"
- board text added: "3V3"
- board text added: "4"
- board text added: "5"
- board text added: "5V"
- board text added: "6"
- board text added: "7"
- board text added: "8"
- board text added: "A0"
- board text added: "A1"
- board text added: "A2"
- board text added: "ADC"
- board text added: "Body Computer"
- board text added: "DAC/ADC"
- board text added: "Design: Wojciech Grzeliński"
- board text added: "EEPROM"
- board text added: "Enc button"
- board text added: "Encoder A/B"
- board text added: "FAN1"
- board text added: "FAN2"
- board text added: "GND"
- board text added: "GPIO"
- board text added: "GPS"
- board text added: "I2C/SPI"
- board text added: "LCD (I2C)"
- board text added: "MicroSD"
- board text added: "NodeMCU EXT"
- board text added: "NodeMCU v3"
- board text added: "PWM"
- board text added: "SWCLK"
- board text added: "SWDIO"
- board text added: "Ver. 1.0"
- board text added: "Vin"

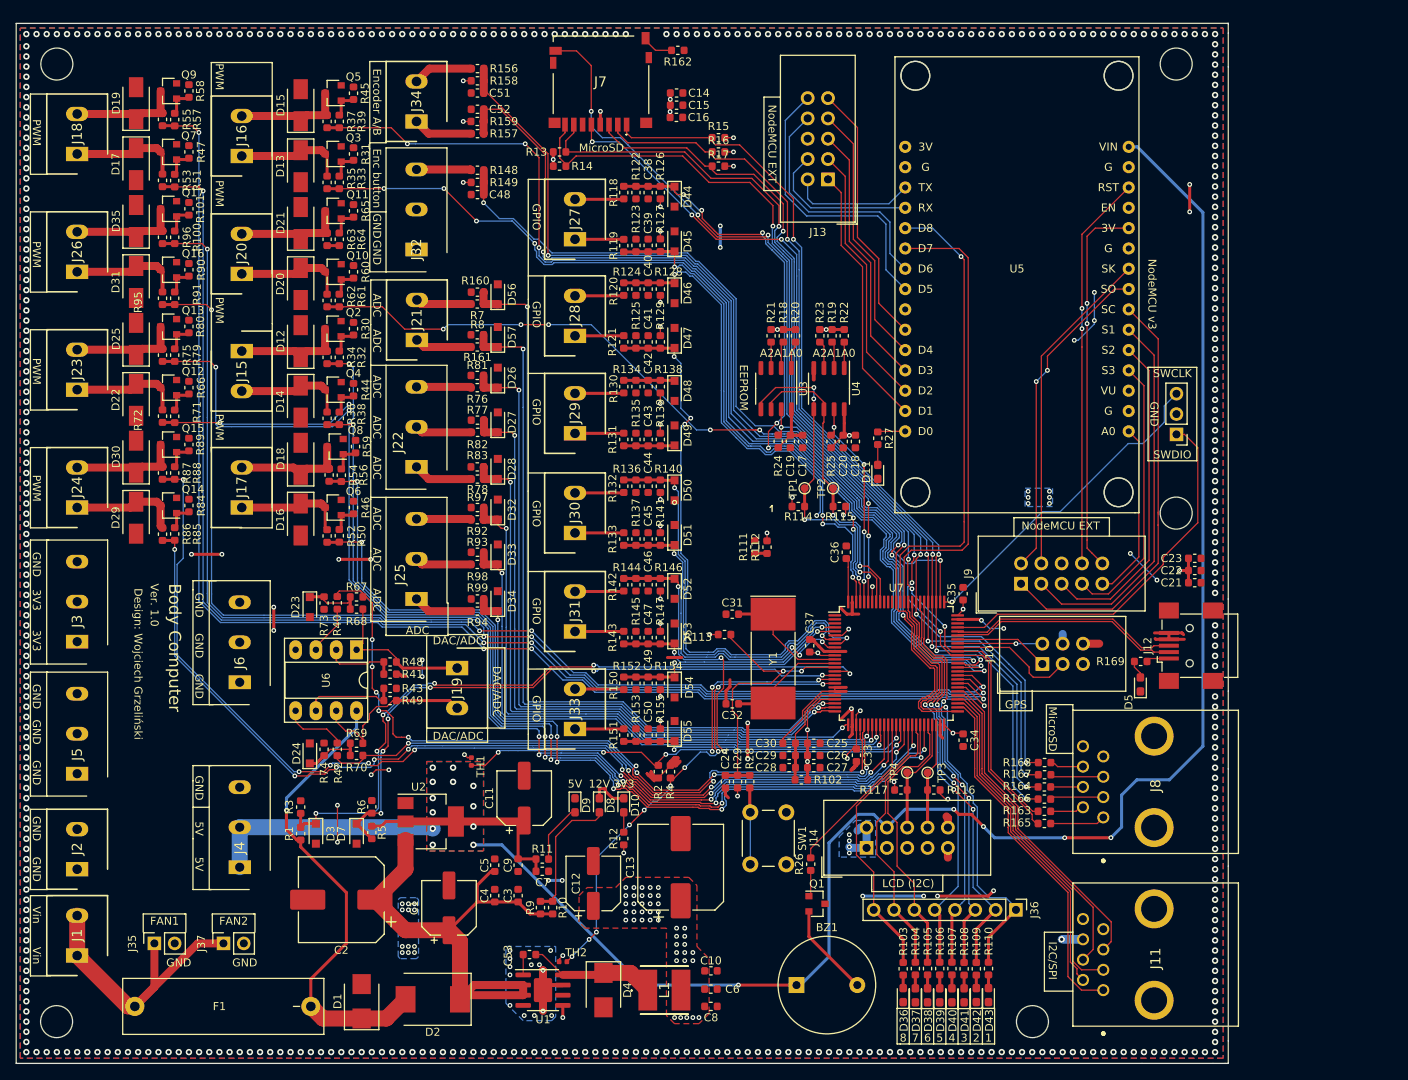
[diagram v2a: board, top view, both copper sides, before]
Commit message: Body Computer - 4layer
Added 4-layer board layout, changed schematic a bit, added jumper for NodeMCU powering, control MOSFET for Fans
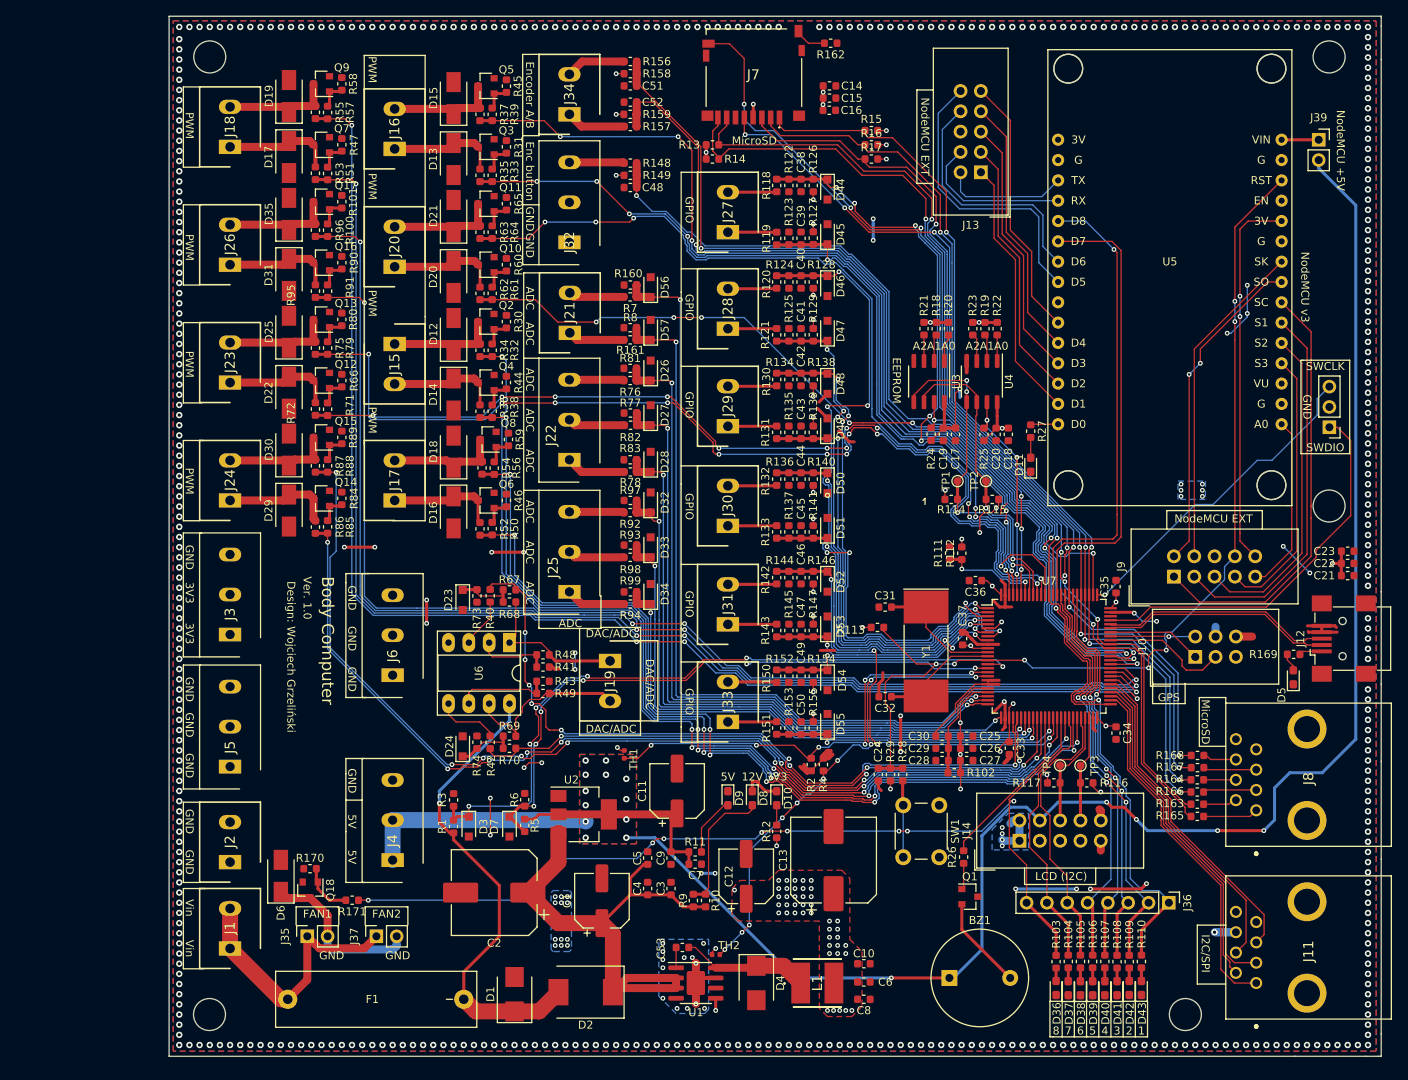
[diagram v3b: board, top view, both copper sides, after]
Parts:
- added D6: D, Diode_SMD:D_SMA, F.Cu at (33.1, 126.6)
- added J39: Conn_01x02, Connector_PinSocket_2.54mm:PinSocket_1x02_P2.54mm_Vertical, F.Cu at (162.8, 34.5)
- added Q18: IRLML2060, Package_TO_SOT_SMD:SOT-23, F.Cu at (36.8, 128.3)
- added R170: 10k, Resistor_SMD:R_0603_1608Metric, F.Cu at (36.7, 125.7)
- added R171: 100, Resistor_SMD:R_0603_1608Metric, F.Cu at (42.0, 129.6)
- moved R111 24.4 mm to (116.7, 86.2)
- moved R112 24.4 mm to (118.2, 86.2)
- moved C21 19.1 mm to (166.4, 89.0)
- moved C22 19.1 mm to (166.4, 87.5)
- moved C23 19.1 mm to (166.4, 86.0)
- moved D5 19.1 mm to (159.6, 101.7)
- moved J38 19.1 mm to (164.1, 70.5)
- moved J8 19.1 mm to (155.0, 118.4)
- moved R117 19.1 mm to (129.7, 114.9)
- moved R167 19.1 mm to (147.7, 113.0)
- moved R168 19.1 mm to (147.7, 111.5)
- moved J11 19.1 mm to (155.0, 140.0)
- moved C1 19.1 mm to (73.2, 129.7)
- moved R41 19.1 mm to (65.8, 100.5)
- moved R43 19.1 mm to (65.8, 102.2)
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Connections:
- J35 pad 2: GND -> Net-(D6-Pad1)
- J37 pad 2: GND -> Net-(D6-Pad1)
- U5 pad 15: +5V -> Net-(J39-Pad1)
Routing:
- net /Inputs_Outputs/MOSFET_OUT_6: track 1.52 -> 111.5 mm, vias 0 -> 6
- net /Inputs_Outputs/MOSFET_OUT_8: track 31.8 -> 125.1 mm, vias 2 -> 10
- net /Inputs_Outputs/MOSFET_OUT_7: track 24.5 -> 117.6 mm, vias 2 -> 10
- net /MCU/Diag_LED_8: track 34.8 -> 122.6 mm, vias 0 -> 8
- net /GPIO/GPIO_3: track 6.86 -> 63.9 mm, vias 0 -> 4
- net /GPIO/GPIO_4: track 6.37 -> 54.8 mm, vias 0 -> 2
- net /MCU/NRST: track 86.2 -> 126.5 mm, vias 4 -> 7
- net /GPIO/GPIO_9: track 50.1 -> 87.0 mm, vias 2 -> 6
- net Net-(D6-Pad1): track 0.00 -> 21.1 mm
- net Net-(R111-Pad1): track 3.47 -> 13.1 mm, vias 1 -> 2
- net +3V3: track 124.4 -> 131.7 mm, vias 99 -> 102
- net Net-(Q18-Pad1): track 0.00 -> 6.67 mm
- net GND: track 131.0 -> 136.2 mm
- net +5V: track 262.6 -> 257.5 mm
- net Net-(J39-Pad1): track 0.00 -> 4.64 mm
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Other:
- board text added: "NodeMCU +5V"
